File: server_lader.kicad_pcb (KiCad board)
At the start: 2 copper layers, 100 x 80 mm, 77 parts, among them IC1 ATMEGA168PA-A, IC2 DAC8560, P1 5V_Vbatt, P10 DISPLAY_STECKER, P11 on/off, P12 A_regulation_out, P2 DISPLAY_STECKER, P3 CONN_02X03, P4 I2C, P5 IP+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

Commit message: kleine Änderungen
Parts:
- removed display_board: EuroBoard_viertel_Type-I_80mmX50mm_holes, EuroBoard_Outline:EuroBoard_viertel_Type-I_80mmX50mm_holes
- removed main: EuroBoard_halb_Type-I_100mmX80mm_holes, EuroBoard_Outline:EuroBoard_halb_Type-I_100mmX80mm_holes
- added Outl: EuroBoard160mmX100mm, EuroBoard_Outline:EuroBoard160mmX100mm, F.Cu at (162.6, 173.4)
- moved C10 112.7 mm to (123.6, 124.6)
- moved C9 112.7 mm to (122.8, 130.7)
- moved P2 112.7 mm to (103.5, 120.5)
- moved P9 112.7 mm to (118.2, 121.0)
- moved C27 112.7 mm to (97.4, 129.9)
- moved C6 112.7 mm to (127.6, 129.7)
- moved C7 112.7 mm to (86.0, 132.7)
- moved C8 112.7 mm to (127.9, 124.3)
- moved DISP1 112.7 mm to (113.7, 147.7)
- moved R11 112.7 mm to (126.1, 124.3)
- moved P6 34.0 mm to (105.8, 47.2)
- moved C24 34.0 mm to (125.2, 73.2)
- moved C26 34.0 mm to (116.6, 72.9)
- moved C4 34.0 mm to (101.6, 76.5)
- moved C5 34.0 mm to (87.6, 41.9)
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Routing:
- net Net-(P6-Pad1): track 17.2 -> 19.6 mm
- net Net-(P5-Pad1): track 17.2 -> 19.2 mm
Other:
- board size 100 x 80 mm -> 100 x 160 mm

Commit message: bugfixes
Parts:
- P9: moved to B.Cu

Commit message: für Fertigung vorbereitet
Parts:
- removed the Outl at (162.6, 173.4)
- added Outl: EuroBoard_halb_Type-I_100mmX80mm_holes, EuroBoard_Outline:EuroBoard_halb_Type-I_100mmX80mm_holes, F.Cu at (62.5, 192.3)
- added Outl: EuroBoard_halb_Type-I_100mmX80mm_holes, EuroBoard_Outline:EuroBoard_halb_Type-I_100mmX80mm_holes, F.Cu at (62.5, 109.9)
- moved C10 7.87 mm to (123.6, 132.5)
- moved C27 7.87 mm to (97.4, 137.8)
- moved C6 7.87 mm to (127.6, 137.5)
- moved C7 7.87 mm to (86.0, 140.6)
- moved C8 7.87 mm to (127.9, 132.2)
- moved C9 7.87 mm to (122.8, 138.6)
- moved DISP1 7.87 mm to (113.7, 155.6)
- moved P2 7.87 mm to (103.5, 128.4)
- moved P9 7.87 mm to (118.2, 128.9)
- moved R11 7.87 mm to (126.1, 132.2)
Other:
- board size 100 x 160 mm -> 100 x 80 mm
- board text added: "Toni B. Server Lader v1.0"

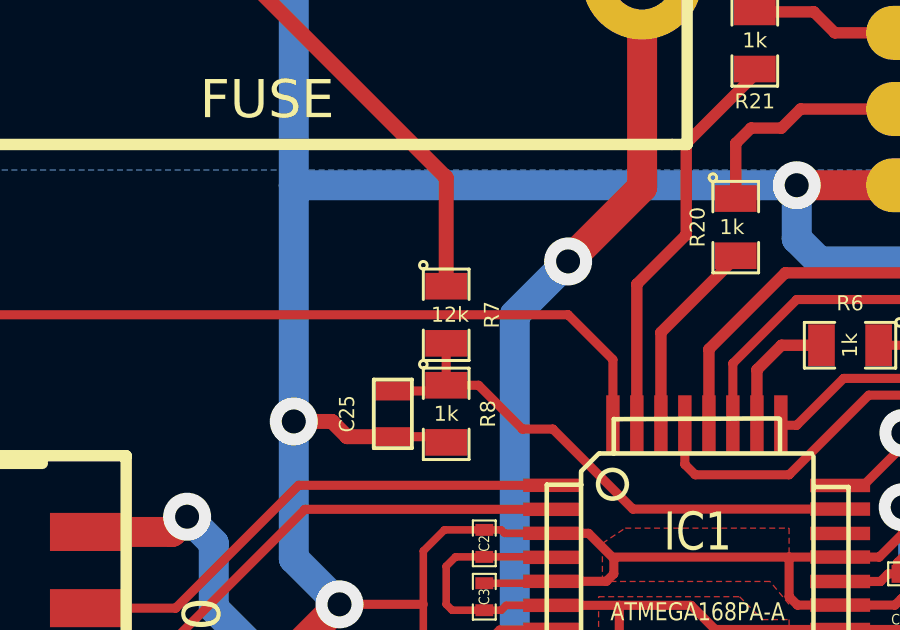
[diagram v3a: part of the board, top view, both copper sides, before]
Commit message: Datenblätter und Schaltplananpassungen wegen neuem OPV im Ausgangszweig
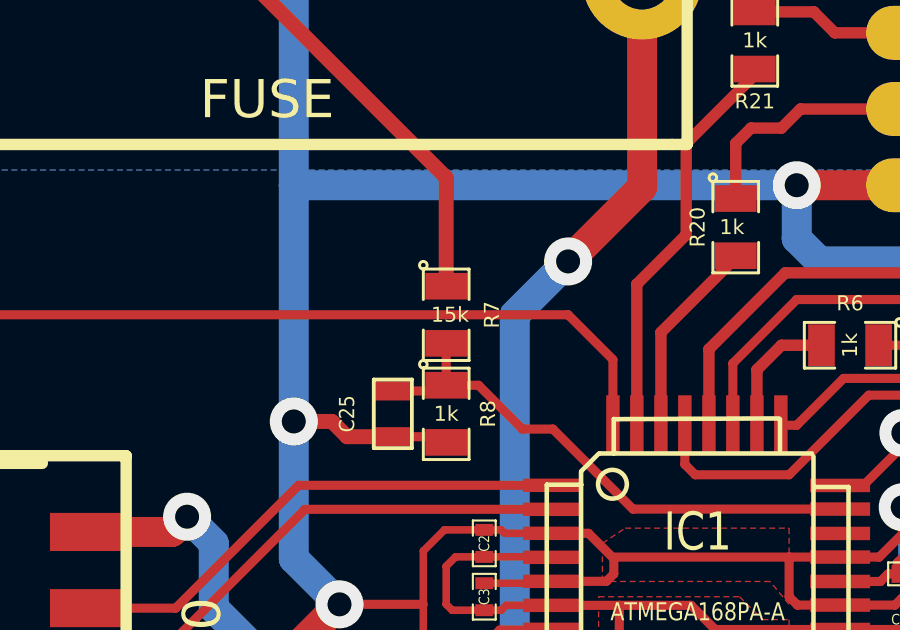
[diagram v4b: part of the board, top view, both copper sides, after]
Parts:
- C4: value 100uF -> 100nF
- R14: value R1 -> 33k
- R15: value R2 -> 10k
- R7: value 12k -> 15k
- U6: value OPA188 -> OPA827
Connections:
- DISP1 pad 21: Net-(DISP1-Pad21) -> (no net)
- DISP1 pad 22: Net-(DISP1-Pad22) -> (no net)
- IC1 pad 13: Net-(IC1-Pad13) -> (no net)
- IC1 pad 22: Net-(IC1-Pad22) -> (no net)
- P12 pad 3: Net-(P12-Pad3) -> (no net)
- P2 pad 7: /MISO_D -> (no net)
- U3 pad 11: Net-(U3-Pad11) -> (no net)
- U3 pad 6: Net-(U3-Pad6) -> (no net)
- U5 pad 3: Net-(U5-Pad3) -> (no net)
- U5 pad 7: Net-(U5-Pad7) -> (no net)
- U7 pad 3: Net-(U7-Pad3) -> (no net)

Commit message: logo hinzugefügt
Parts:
- added G***: LOGO, Toni:Kupferdickbutt, F.Cu at (103.5, 156.8)
